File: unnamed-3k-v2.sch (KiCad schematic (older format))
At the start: 31 parts, among them SW1 SW_Push, U1 ATmega32U2-AU, U2 PRTR5V0U2X, Y1 Crystal_GND24_Small

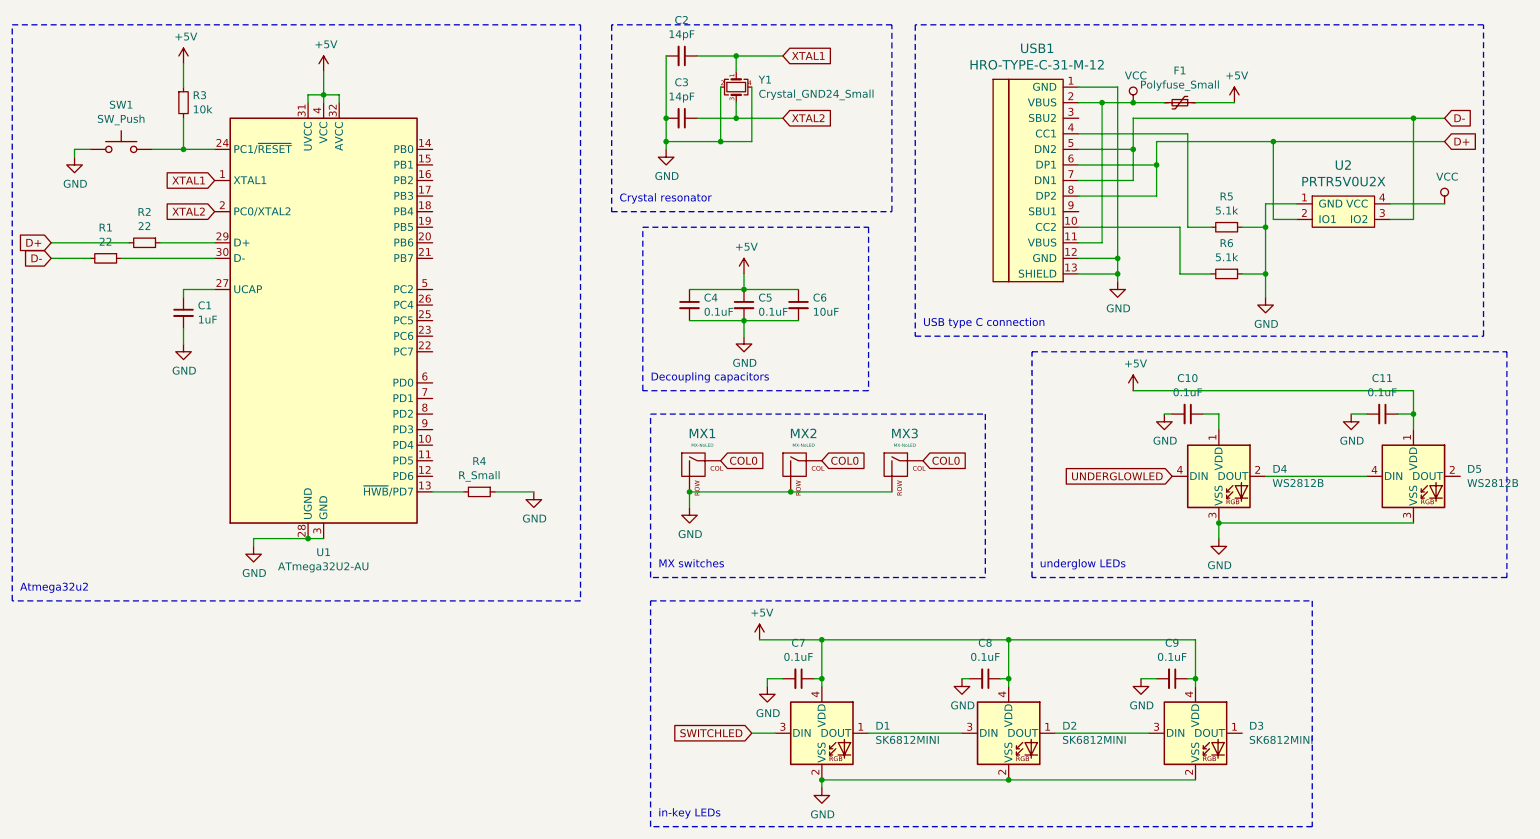
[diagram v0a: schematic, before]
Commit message: PCB design and laser files finished
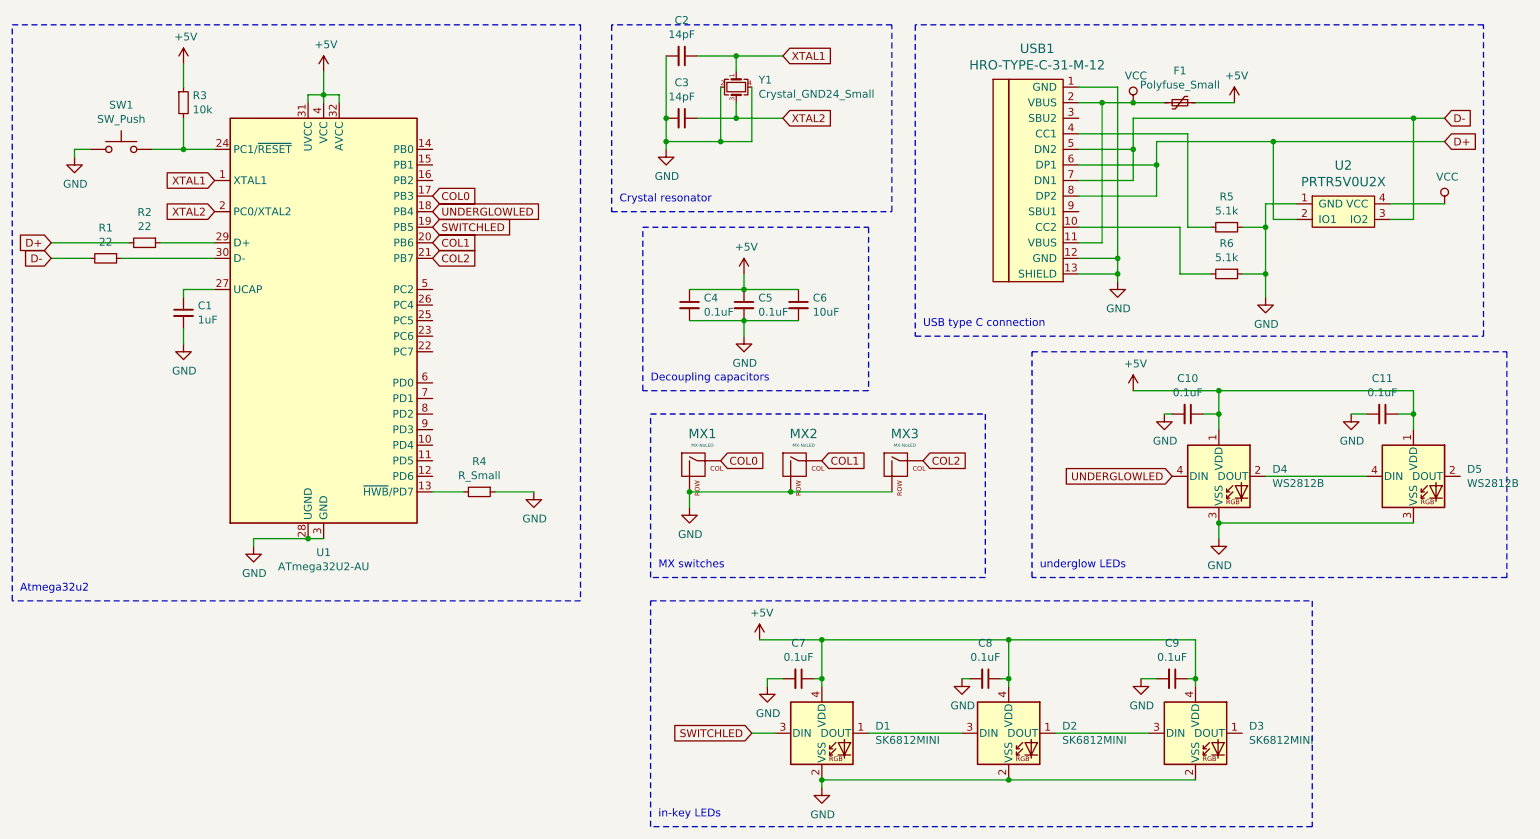
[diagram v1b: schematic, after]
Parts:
- D1, D2, D3: footprint LED_SMD:LED_SK6812MINI_PLCC4_3.5x3.5mm_P1.75mm -> Keebio-Parts:SK6812-MINI-E
- MX1, MX2, MX3: footprint (none) -> MX_Only:MXOnly-1U-Hotswap
- R1, R2, R3, R4, R5, R6: footprint (none) -> Resistor_SMD:R_0805_2012Metric_Pad1.15x1.40mm_HandSolder
- SW1: footprint (none) -> random-keyboard-parts:SKQGADE010
- U2: footprint (none) -> random-keyboard-parts:SOT143B
- USB1: footprint (none) -> Type-C:HRO-TYPE-C-31-M-12-HandSoldering
- Y1: footprint (none) -> Crystal:Crystal_SMD_3225-4Pin_3.2x2.5mm_HandSoldering
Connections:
- net +5V: now also C10.1, D4.1 (VDD)
- net COL0: now also U1.17 (PB3); no longer MX2.1 (COL), MX3.1 (COL)
- net SWITCHLED: now also U1.19 (PB5)
- net UNDERGLOWLED: now also U1.18 (PB4)
- net COL1: now reaches U1.20 (PB6)
- net COL1: now also MX2.1 (COL)
- net COL2: now reaches U1.21 (PB7)
- net COL2: now also MX3.1 (COL)
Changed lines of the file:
@@
 F 0 "R4" V 3854 3700 50  0000 C CNN
 F 1 "R_Small" V 3945 3700 50  0000 C CNN
-F 2 "" H 4050 3700 50  0001 C CNN
+F 2 "Resistor_SMD:R_0805_2012Metric_Pad1.15x1.40mm_HandSolder" H 4050 3700 50  0001 C CNN
 F 3 "~" H 4050 3700 50  0001 C CNN
 	1    4050 3700
@@
 F 0 "R2" V 1704 2100 50  0000 C CNN
 F 1 "22" V 1795 2100 50  0000 C CNN
-F 2 "" H 1900 2100 50  0001 C CNN
+F 2 "Resistor_SMD:R_0805_2012Metric_Pad1.15x1.40mm_HandSolder" H 1900 2100 50  0001 C CNN
 F 3 "~" H 1900 2100 50  0001 C CNN
 	1    1900 2100
@@
 F 0 "R1" V 1454 2200 50  0000 C CNN
 F 1 "22" V 1545 2200 50  0000 C CNN
-F 2 "" H 1650 2200 50  0001 C CNN
+F 2 "Resistor_SMD:R_0805_2012Metric_Pad1.15x1.40mm_HandSolder" H 1650 2200 50  0001 C CNN
 F 3 "~" H 1650 2200 50  0001 C CNN
 	1    1650 2200
@@
 F 0 "SW1" H 1750 1785 50  0000 C CNN
 F 1 "SW_Push" H 1750 1694 50  0000 C CNN
-F 2 "" H 1750 1700 50  0001 C CNN
+F 2 "random-keyboard-parts:SKQGADE010" H 1750 1700 50  0001 C CNN
 F 3 "~" H 1750 1700 50  0001 C CNN
 	1    1750 1500
@@
 F 0 "R3" H 2209 1246 50  0000 L CNN
 F 1 "10k" H 2209 1155 50  0000 L CNN
-F 2 "" H 2150 1200 50  0001 C CNN
+F 2 "Resistor_SMD:R_0805_2012Metric_Pad1.15x1.40mm_HandSolder" H 2150 1200 50  0001 C CNN
 F 3 "~" H 2150 1200 50  0001 C CNN
 	1    2150 1200
@@
 F 0 "Y1" V 5654 1244 50  0000 L CNN
 F 1 "Crystal_GND24_Small" V 5745 1244 50  0000 L CNN
-F 2 "" H 5700 1100 50  0001 C CNN
+F 2 "Crystal:Crystal_SMD_3225-4Pin_3.2x2.5mm_HandSoldering" H 5700 1100 50  0001 C CNN
 F 3 "~" H 5700 1100 50  0001 C CNN
 	1    5700 1100
@@
 F 0 "USB1" H 7633 2447 60  0000 C CNN
 F 1 "HRO-TYPE-C-31-M-12" H 7633 2341 60  0000 C CNN
-F 2 "" H 7800 1650 60  0001 C CNN
+F 2 "Type-C:HRO-TYPE-C-31-M-12-HandSoldering" H 7800 1650 60  0001 C CNN
 F 3 "" H 7800 1650 60  0001 C CNN
 	1    7800 1650
@@
 F 0 "U2" H 9600 2197 60  0000 C CNN
 F 1 "PRTR5V0U2X" H 9600 2091 60  0000 C CNN
-F 2 "" H 9600 1900 60  0001 C CNN
+F 2 "random-keyboard-parts:SOT143B" H 9600 1900 60  0001 C CNN
 F 3 "" H 9600 1900 60  0001 C CNN
 	1    9600 1900
@@
 F 0 "R5" V 8654 2000 50  0000 C CNN
 F 1 "5.1k" V 8745 2000 50  0000 C CNN
-F 2 "" H 8850 2000 50  0001 C CNN
+F 2 "Resistor_SMD:R_0805_2012Metric_Pad1.15x1.40mm_HandSolder" H 8850 2000 50  0001 C CNN
 F 3 "~" H 8850 2000 50  0001 C CNN
 	1    8850 2000
@@
 F 0 "R6" V 8654 2300 50  0000 C CNN
 F 1 "5.1k" V 8745 2300 50  0000 C CNN
-F 2 "" H 8850 2300 50  0001 C CNN
+F 2 "Resistor_SMD:R_0805_2012Metric_Pad1.15x1.40mm_HandSolder" H 8850 2300 50  0001 C CNN
 F 3 "~" H 8850 2300 50  0001 C CNN
 	1    8850 2300
@@
 F 0 "MX1" H 5483 3773 60  0000 C CNN
 F 1 "MX-NoLED" H 5483 3699 20  0000 C CNN
-F 2 "" H 4825 3525 60  0001 C CNN
+F 2 "MX_Only:MXOnly-1U-Hotswap" H 4825 3525 60  0001 C CNN
 F 3 "" H 4825 3525 60  0001 C CNN
 	1    5450 3550
@@
 F 0 "MX2" H 6133 3773 60  0000 C CNN
 F 1 "MX-NoLED" H 6133 3699 20  0000 C CNN
-F 2 "" H 5475 3525 60  0001 C CNN
+F 2 "MX_Only:MXOnly-1U-Hotswap" H 5475 3525 60  0001 C CNN
 F 3 "" H 5475 3525 60  0001 C CNN
 	1    6100 3550
@@
 F 0 "MX3" H 6783 3773 60  0000 C CNN
 F 1 "MX-NoLED" H 6783 3699 20  0000 C CNN
-F 2 "" H 6125 3525 60  0001 C CNN
+F 2 "MX_Only:MXOnly-1U-Hotswap" H 6125 3525 60  0001 C CNN
 F 3 "" H 6125 3525 60  0001 C CNN
 	1    6750 3550
@@
 COL0
 Text GLabel 6250 3500 2    50   Input ~ 0
-COL0
+COL1
 Text GLabel 6900 3500 2    50   Input ~ 0
-COL0
+COL2
 $Comp
 L power:GND #PWR0115
@@
 F 0 "D1" H 6594 5296 50  0000 L CNN
 F 1 "SK6812MINI" H 6594 5205 50  0000 L CNN
-F 2 "LED_SMD:LED_SK6812MINI_PLCC4_3.5x3.5mm_P1.75mm" H 6300 4950 50  0001 L TNN
+F 2 "Keebio-Parts:SK6812-MINI-E" H 6300 4950 50  0001 L TNN
 F 3 "https://cdn-shop.adafruit.com/product-files/2686/SK6812MINI_REV.01-1-2.pdf" H 6350 4875 50  0001 L TNN
 	1    6250 5250
@@
 F 0 "D2" H 7794 5296 50  0000 L CNN
 F 1 "SK6812MINI" H 7794 5205 50  0000 L CNN
-F 2 "LED_SMD:LED_SK6812MINI_PLCC4_3.5x3.5mm_P1.75mm" H 7500 4950 50  0001 L TNN
+F 2 "Keebio-Parts:SK6812-MINI-E" H 7500 4950 50  0001 L TNN
 F 3 "https://cdn-shop.adafruit.com/product-files/2686/SK6812MINI_REV.01-1-2.pdf" H 7550 4875 50  0001 L TNN
 	1    7450 5250
@@
 F 0 "D3" H 8994 5296 50  0000 L CNN
 F 1 "SK6812MINI" H 8994 5205 50  0000 L CNN
-F 2 "LED_SMD:LED_SK6812MINI_PLCC4_3.5x3.5mm_P1.75mm" H 8700 4950 50  0001 L TNN
+F 2 "Keebio-Parts:SK6812-MINI-E" H 8700 4950 50  0001 L TNN
 F 3 "https://cdn-shop.adafruit.com/product-files/2686/SK6812MINI_REV.01-1-2.pdf" H 8750 4875 50  0001 L TNN
 	1    8650 5250
@@
 $EndComp
 Wire Wire Line
-	8250 3050 10050 3050
+	8250 3050 8800 3050
 Wire Wire Line
 	10050 3050 10050 3200
@@
 Wire Wire Line
 	8800 3300 8800 3200
-Wire Wire Line
-	8800 3200 8700 3200
 $Comp
 L power:GND #PWR0123
@@
 Text Notes 1100 4350 0    50   ~ 0
 Atmega32u2
+Wire Wire Line
+	8700 3200 8800 3200
+Wire Wire Line
+	8800 3200 8800 3050
+Connection ~ 8800 3200
+Connection ~ 8800 3050
+Wire Wire Line
+	8800 3050 10050 3050
+Text GLabel 3750 1900 2    50   Input ~ 0
+UNDERGLOWLED
+Text GLabel 3750 2000 2    50   Input ~ 0
+SWITCHLED
+Text GLabel 3750 1800 2    50   Input ~ 0
+COL0
+Text GLabel 3750 2100 2    50   Input ~ 0
+COL1
+Text GLabel 3750 2200 2    50   Input ~ 0
+COL2
 $EndSCHEMATC

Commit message: everything else
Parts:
- R4: value R_Small -> 10k
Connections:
- net COL0: now also U1.18 (PB4); no longer U1.17 (PB3)
- net UNDERGLOWLED: now also U1.17 (PB3); no longer U1.18 (PB4)
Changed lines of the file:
@@
 EESchema Schematic File Version 4
+LIBS:unnamed-3k-v2-cache
 EELAYER 30 0
 EELAYER END
@@
 P 4050 3700
 F 0 "R4" V 3854 3700 50  0000 C CNN
-F 1 "R_Small" V 3945 3700 50  0000 C CNN
+F 1 "10k" V 3945 3700 50  0000 C CNN
 F 2 "Resistor_SMD:R_0805_2012Metric_Pad1.15x1.40mm_HandSolder" H 4050 3700 50  0001 C CNN
 F 3 "~" H 4050 3700 50  0001 C CNN
@@
 Wire Wire Line
 	8800 3050 10050 3050
-Text GLabel 3750 1900 2    50   Input ~ 0
+Text GLabel 3750 1800 2    50   Input ~ 0
 UNDERGLOWLED
 Text GLabel 3750 2000 2    50   Input ~ 0
 SWITCHLED
-Text GLabel 3750 1800 2    50   Input ~ 0
+Text GLabel 3750 1900 2    50   Input ~ 0
 COL0
 Text GLabel 3750 2100 2    50   Input ~ 0
